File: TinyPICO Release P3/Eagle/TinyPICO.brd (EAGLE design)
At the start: 31.9 x 17.8 mm, 37 parts, among them IC2 CP2104, Q3 MUN5214DW1T1G, T2 TINYPICO-P-FETKMB, U1 NCP170AMX300TCG

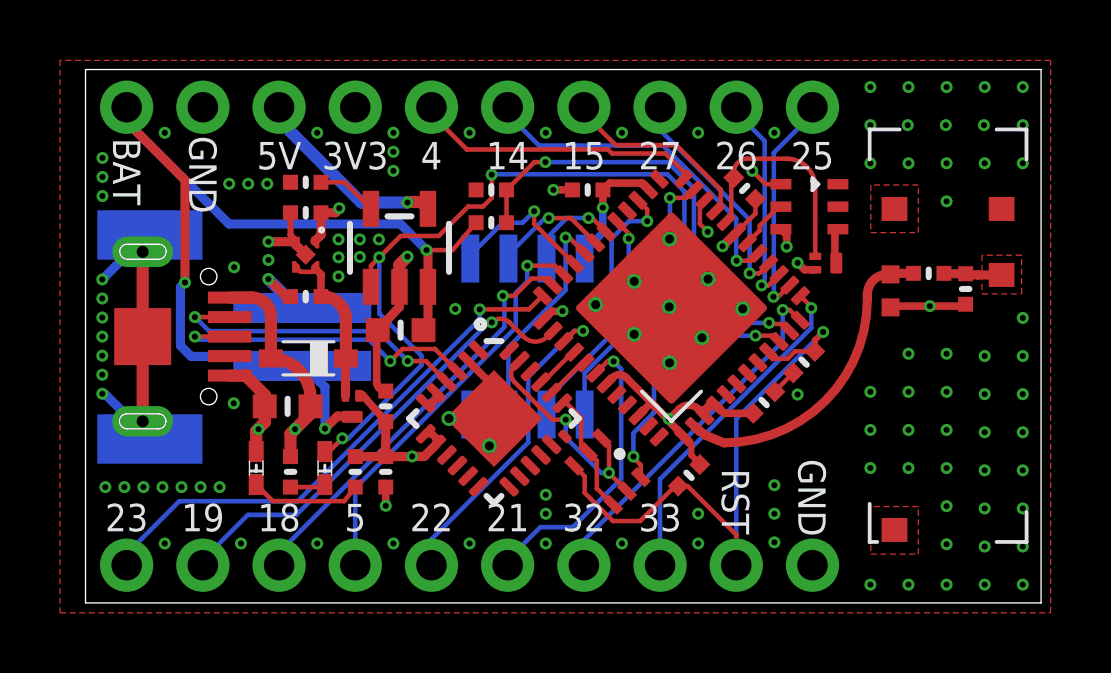
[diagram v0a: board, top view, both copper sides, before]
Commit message: Fixed PSRAM silk no back of the bopard Fixed positions of the Inductor and Cap on the matching network Updated schematic PDF
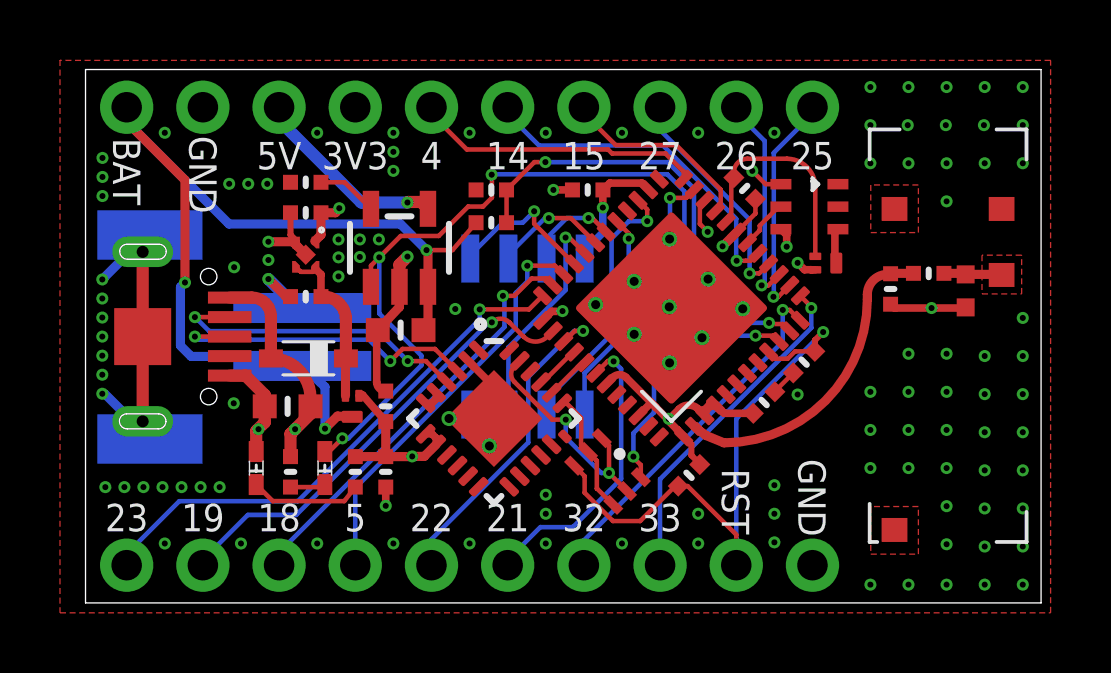
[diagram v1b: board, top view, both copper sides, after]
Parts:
- D1: value (none) -> RED
- D3: value (none) -> ORANGE
- moved C4 2.50 mm to (26.7, 11.4)
- moved L1 2.50 mm to (29.2, 11.4)
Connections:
- net ANT: now also L1.2; no longer C4.1
- net LNA_IN: now also C4.1; no longer L1.2
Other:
- board text added: "PSRAM"
